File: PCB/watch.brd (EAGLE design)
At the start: 81.1 x 53.1 mm, 58 parts, among them IC1 ISL1209, J2 USB-MICROB, Q1 32.768 KHz, T1 BC850, U2 MKL27Z256VLH4

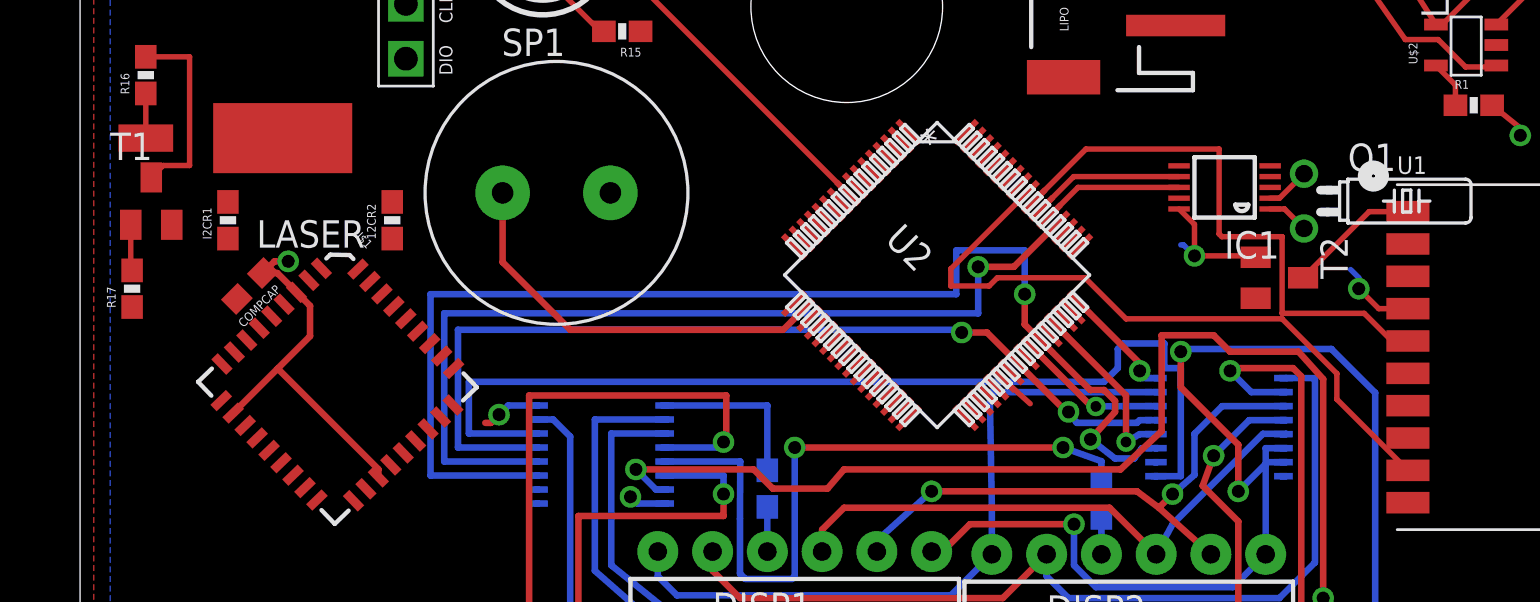
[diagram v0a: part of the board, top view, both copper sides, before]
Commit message: laser wired
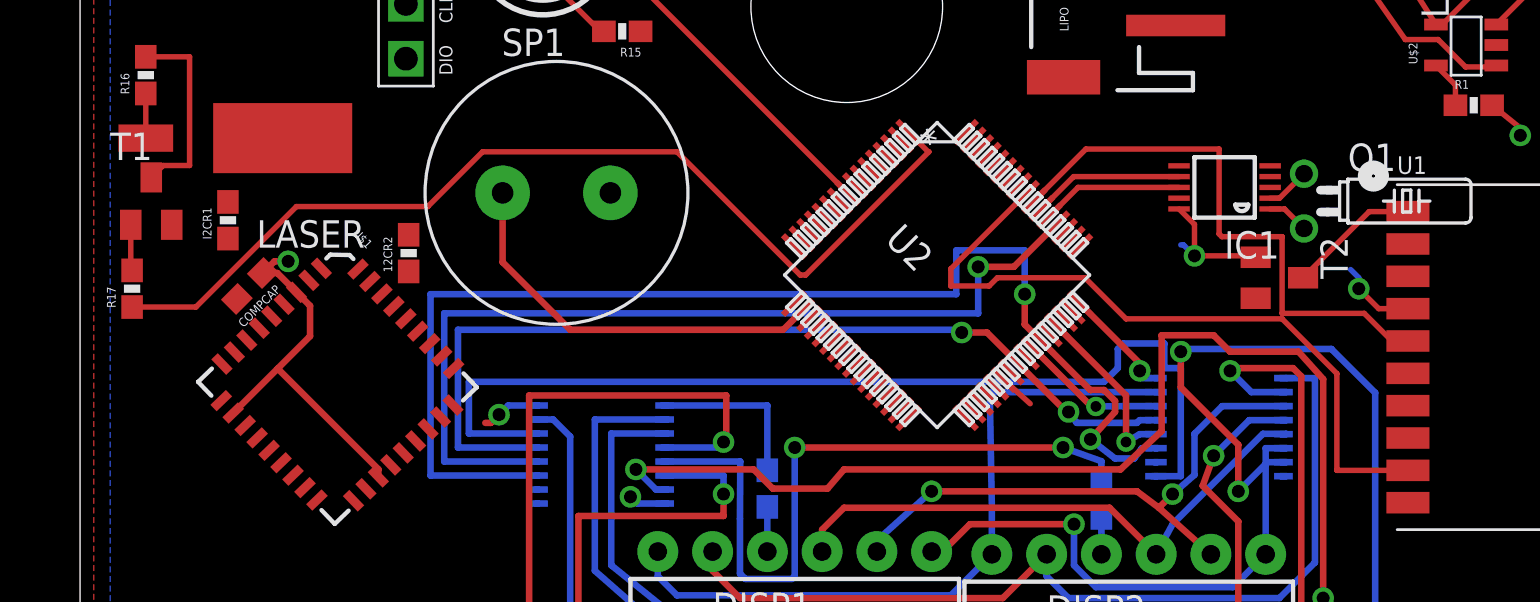
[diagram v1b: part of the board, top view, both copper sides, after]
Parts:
- moved 12CR2 1.70 mm to (26.2, 42.9)
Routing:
- net PTE0: track 0.00 -> 46.0 mm
- net PTC11: track 31.5 -> 33.5 mm
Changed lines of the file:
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@@
 </autorouter>
 <elements>
-<element name="12CR2" library="SparkFun-Resistors" package="0603-RES" value="10K" x="25.4" y="44.45" rot="R90"/>
+<element name="12CR2" library="SparkFun-Resistors" package="0603-RES" value="10K" x="26.162" y="42.926" rot="R90"/>
 <element name="C1" library="SparkFun" package="0603" value=".1uf" x="-41.91" y="73.66"/>
 <element name="C2" library="SparkFun" package="0603" value=".1uf" x="-45.72" y="73.66"/>
@@
 <wire x1="29.718" y1="35.052" x2="24.758084375" y2="32.899915625" width="0" layer="19" extent="1-1"/>
 <wire x1="57.302134375" y1="40.584171875" x2="61.976" y2="43.307" width="0" layer="19" extent="1-16"/>
-<wire x1="25.4" y1="45.3" x2="20.574" y2="42.545" width="0" layer="19" extent="1-1"/>
+<wire x1="26.162" y1="43.776" x2="20.574" y2="42.545" width="0" layer="19" extent="1-1"/>
 <wire x1="48.640065625" y1="35.98796875" x2="57.302134375" y2="40.584171875" width="0" layer="19" extent="1-1"/>
 <wire x1="45.104521875" y1="44.29648125" x2="48.640065625" y2="35.98796875" width="0" layer="19" extent="1-1"/>
@@
 <wire x1="57.2118875" y1="45.974" x2="55.887921875" y2="44.650034375" width="0.254" layer="1"/>
 <wire x1="26.030421875" y1="39.880965625" x2="55.887921875" y2="44.650034375" width="0" layer="19" extent="1-1"/>
-<wire x1="25.4" y1="43.6" x2="26.030421875" y2="39.880965625" width="0" layer="19" extent="1-1"/>
+<wire x1="26.162" y1="42.076" x2="26.030421875" y2="39.880965625" width="0" layer="19" extent="1-1"/>
 </signal>
 <signal name="PTC9">
@@
 <contactref element="R17" pad="1"/>
 <contactref element="U2" pad="1"/>
-<wire x1="13.335" y1="40.425" x2="49.347171875" y2="48.539134375" width="0" layer="19" extent="1-1"/>
+<wire x1="13.335" y1="40.425" x2="16.295" y2="40.425" width="0.254" layer="1"/>
+<wire x1="16.295" y1="40.425" x2="20.955" y2="45.085" width="0.254" layer="1"/>
+<wire x1="29.591" y1="47.625" x2="38.608" y2="47.625" width="0.254" layer="1"/>
+<wire x1="38.608" y1="47.625" x2="44.323" y2="41.91" width="0.254" layer="1"/>
+<wire x1="44.323" y1="41.91" x2="44.577" y2="41.91" width="0.254" layer="1"/>
+<wire x1="44.577" y1="41.91" x2="50.292" y2="47.625" width="0.254" layer="1"/>
+<wire x1="50.292" y1="47.625" x2="50.26130625" y2="47.625" width="0.254" layer="1"/>
+<wire x1="50.26130625" y1="47.625" x2="49.347171875" y2="48.539134375" width="0.254" layer="1"/>
+<wire x1="20.955" y1="45.085" x2="27.051" y2="45.085" width="0.254" layer="1"/>
+<wire x1="27.051" y1="45.085" x2="29.591" y2="47.625" width="0.254" layer="1"/>
 </signal>
 <signal name="PTA18">
@@
 <contactref element="U1" pad="P$9"/>
 <contactref element="U2" pad="56"/>
-<wire x1="72.51" y1="32.85" x2="69.215" y2="36.145" width="0.254" layer="1"/>
-<wire x1="69.215" y1="36.145" x2="69.215" y2="37.338" width="0.254" layer="1"/>
 <wire x1="69.215" y1="37.338" x2="66.675" y2="39.878" width="0.254" layer="1"/>
 <wire x1="66.675" y1="39.878" x2="59.436" y2="39.878" width="0.254" layer="1"/>
@@
 <wire x1="51.308" y1="41.402" x2="51.308" y2="42.1914625" width="0.254" layer="1"/>
 <wire x1="51.308" y1="42.1914625" x2="54.827246875" y2="45.710709375" width="0.254" layer="1"/>
+<wire x1="69.215" y1="37.338" x2="69.215" y2="32.85" width="0.254" layer="1"/>
+<wire x1="69.215" y1="32.85" x2="72.51" y2="32.85" width="0.254" layer="1"/>
 </signal>
 </signals>

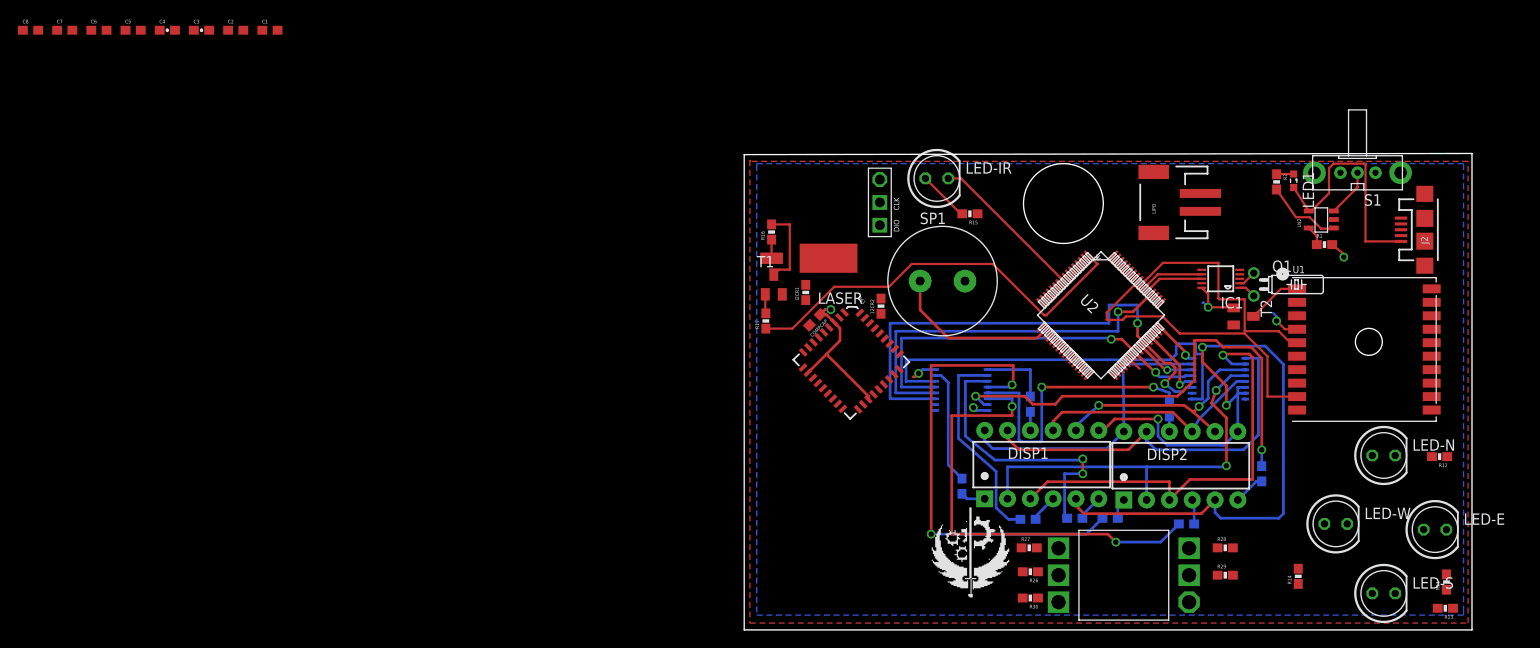
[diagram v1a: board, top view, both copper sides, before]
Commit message: refactored charging circuit and add caps to it
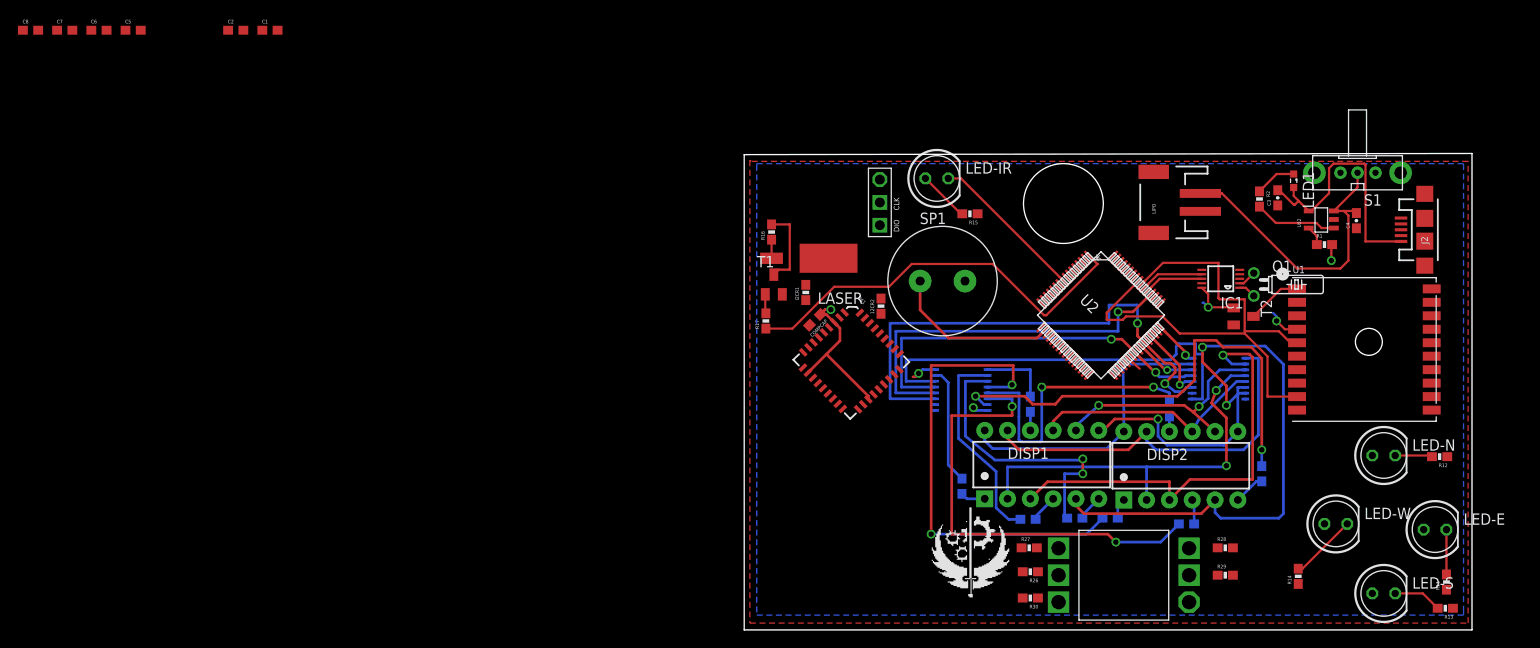
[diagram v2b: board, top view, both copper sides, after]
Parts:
- moved C4 134.1 mm to (79.1, 52.5), turned to 90 degrees
- moved C3 121.3 mm to (70.4, 55.0), turned to 90 degrees
- moved R2 2.69 mm to (68.3, 54.9)
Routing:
- net N$3: track 5.35 -> 34.2 mm
- net N$37: track 0.00 -> 7.53 mm
- net N$38: track 0.00 -> 5.42 mm
- net N$36: track 0.00 -> 4.99 mm
- net N$35: track 0.00 -> 4.16 mm
- net N$4: track 25.8 -> 29.2 mm
- net N$5: track 1.93 -> 4.62 mm
- net N$7: track 8.54 -> 9.27 mm
- net GND: track 4.61 -> 3.89 mm

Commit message: wired compass LEDs. good god this thing is a mess
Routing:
- net PTD2: track 0.00 -> 81.2 mm
- net PTD3: track 0.00 -> 75.6 mm, vias 0 -> 1
- net PTD1: track 0.00 -> 73.4 mm
- net PTD5: track 0.00 -> 70.0 mm, vias 0 -> 1
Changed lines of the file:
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@@
 <contactref element="U2" pad="62"/>
 <contactref element="LED-N" pad="A"/>
-<wire x1="52.70593125" y1="47.832028125" x2="80.899" y2="26.289" width="0" layer="19" extent="1-1"/>
+<wire x1="80.899" y1="26.289" x2="80.899" y2="26.543" width="0.254" layer="16"/>
+<wire x1="80.899" y1="26.543" x2="82.931" y2="28.575" width="0.254" layer="16"/>
+<wire x1="82.931" y1="28.575" x2="87.757" y2="28.575" width="0.254" layer="16"/>
+<wire x1="87.757" y1="28.575" x2="89.408" y2="30.226" width="0.254" layer="16"/>
+<wire x1="89.408" y1="30.226" x2="89.408" y2="49.403" width="0.254" layer="16"/>
+<wire x1="89.408" y1="49.403" x2="86.614" y2="52.197" width="0.254" layer="16"/>
+<wire x1="86.614" y1="52.197" x2="66.929" y2="52.197" width="0.254" layer="16"/>
+<wire x1="66.929" y1="52.197" x2="65.786" y2="51.054" width="0.254" layer="16"/>
+<via x="65.786" y="51.054" extent="1-16" drill="0.6" shape="square"/>
+<wire x1="65.786" y1="51.054" x2="60.706" y2="51.054" width="0.254" layer="1"/>
+<wire x1="60.706" y1="51.054" x2="60.579" y2="51.054" width="0" layer="19" extent="1-16"/>
+<wire x1="52.70593125" y1="47.832028125" x2="54.530903125" y2="49.657" width="0.254" layer="1"/>
+<wire x1="54.530903125" y1="49.657" x2="60.706" y2="49.657" width="0.254" layer="1"/>
+<wire x1="60.706" y1="49.657" x2="60.706" y2="51.054" width="0.254" layer="1"/>
 </signal>
 <signal name="PTD3">
 <contactref element="U2" pad="60"/>
 <contactref element="LED-E" pad="A"/>
-<wire x1="53.413034375" y1="47.124921875" x2="86.614" y2="18.034" width="0" layer="19" extent="1-1"/>
+<wire x1="86.614" y1="18.034" x2="86.614" y2="26.035" width="0.254" layer="16"/>
+<wire x1="86.614" y1="26.035" x2="90.17" y2="29.591" width="0.254" layer="16"/>
+<wire x1="90.17" y1="29.591" x2="90.17" y2="49.657" width="0.254" layer="16"/>
+<wire x1="90.17" y1="49.657" x2="86.106" y2="53.721" width="0.254" layer="16"/>
+<wire x1="86.106" y1="53.721" x2="66.548" y2="53.721" width="0.254" layer="16"/>
+<wire x1="66.548" y1="53.721" x2="64.77" y2="51.943" width="0.254" layer="16"/>
+<wire x1="64.77" y1="51.943" x2="64.77" y2="49.657" width="0.254" layer="16"/>
+<wire x1="64.77" y1="49.657" x2="64.389" y2="49.657" width="0.254" layer="16"/>
+<via x="64.389" y="49.657" extent="1-16" drill="0.6" shape="square"/>
+<wire x1="55.5641125" y1="49.276" x2="53.413034375" y2="47.124921875" width="0.254" layer="1"/>
+<wire x1="55.5641125" y1="49.276" x2="62.865" y2="49.276" width="0.254" layer="1"/>
+<wire x1="62.865" y1="49.276" x2="63.246" y2="49.657" width="0.254" layer="1"/>
+<wire x1="63.246" y1="49.657" x2="64.389" y2="49.657" width="0.254" layer="1"/>
 </signal>
 <signal name="PTD2">
 <contactref element="U2" pad="59"/>
 <contactref element="LED-S" pad="A"/>
-<wire x1="80.899" y1="10.922" x2="53.7665875" y2="46.77136875" width="0" layer="19" extent="1-1"/>
+<wire x1="80.899" y1="10.922" x2="86.614" y2="16.637" width="0.254" layer="1"/>
+<wire x1="86.614" y1="16.637" x2="87.884" y2="16.637" width="0.254" layer="1"/>
+<wire x1="87.884" y1="16.637" x2="88.011" y2="16.764" width="0.254" layer="1"/>
+<wire x1="88.011" y1="16.764" x2="88.011" y2="22.86" width="0.254" layer="1"/>
+<wire x1="88.011" y1="22.86" x2="90.17" y2="25.019" width="0.254" layer="1"/>
+<wire x1="90.17" y1="25.019" x2="90.17" y2="29.718" width="0.254" layer="1"/>
+<wire x1="90.17" y1="29.718" x2="89.408" y2="30.48" width="0.254" layer="1"/>
+<wire x1="89.408" y1="30.48" x2="89.408" y2="48.895" width="0.254" layer="1"/>
+<wire x1="89.408" y1="48.895" x2="89.281" y2="48.768" width="0.254" layer="1"/>
+<wire x1="89.281" y1="48.768" x2="80.645" y2="48.768" width="0.254" layer="1"/>
+<wire x1="80.645" y1="48.768" x2="78.613" y2="46.736" width="0.254" layer="1"/>
+<wire x1="78.613" y1="46.736" x2="71.374" y2="46.736" width="0.254" layer="1"/>
+<wire x1="71.374" y1="46.736" x2="69.342" y2="48.768" width="0.254" layer="1"/>
+<wire x1="69.342" y1="48.768" x2="55.626" y2="48.768" width="0.254" layer="1"/>
+<wire x1="55.626" y1="48.768" x2="53.7665875" y2="46.9085875" width="0.254" layer="1"/>
+<wire x1="53.7665875" y1="46.9085875" x2="53.7665875" y2="46.77136875" width="0.254" layer="1"/>
 </signal>
 <signal name="PTD1">
 <contactref element="U2" pad="58"/>
 <contactref element="LED-W" pad="A"/>
-<wire x1="75.565" y1="18.669" x2="54.120140625" y2="46.41781875" width="0" layer="19" extent="1-1"/>
+<wire x1="75.565" y1="18.669" x2="82.423" y2="25.527" width="0.254" layer="1"/>
+<wire x1="82.423" y1="25.527" x2="82.423" y2="28.829" width="0.254" layer="1"/>
+<wire x1="82.423" y1="28.829" x2="83.058" y2="29.464" width="0.254" layer="1"/>
+<wire x1="83.058" y1="29.464" x2="88.519" y2="29.464" width="0.254" layer="1"/>
+<wire x1="88.519" y1="29.464" x2="89.408" y2="30.353" width="0.254" layer="1"/>
+<wire x1="89.408" y1="30.353" x2="89.408" y2="45.974" width="0.254" layer="1"/>
+<wire x1="89.408" y1="45.974" x2="89.281" y2="46.101" width="0.254" layer="1"/>
+<wire x1="89.281" y1="46.101" x2="70.358" y2="46.101" width="0.254" layer="1"/>
+<wire x1="70.358" y1="46.101" x2="68.072" y2="48.387" width="0.254" layer="1"/>
+<wire x1="68.072" y1="48.387" x2="56.007" y2="48.387" width="0.254" layer="1"/>
+<wire x1="56.007" y1="48.387" x2="54.120140625" y2="46.500140625" width="0.254" layer="1"/>
+<wire x1="54.120140625" y1="46.500140625" x2="54.120140625" y2="46.41781875" width="0.254" layer="1"/>
 </signal>
 <signal name="N$39">

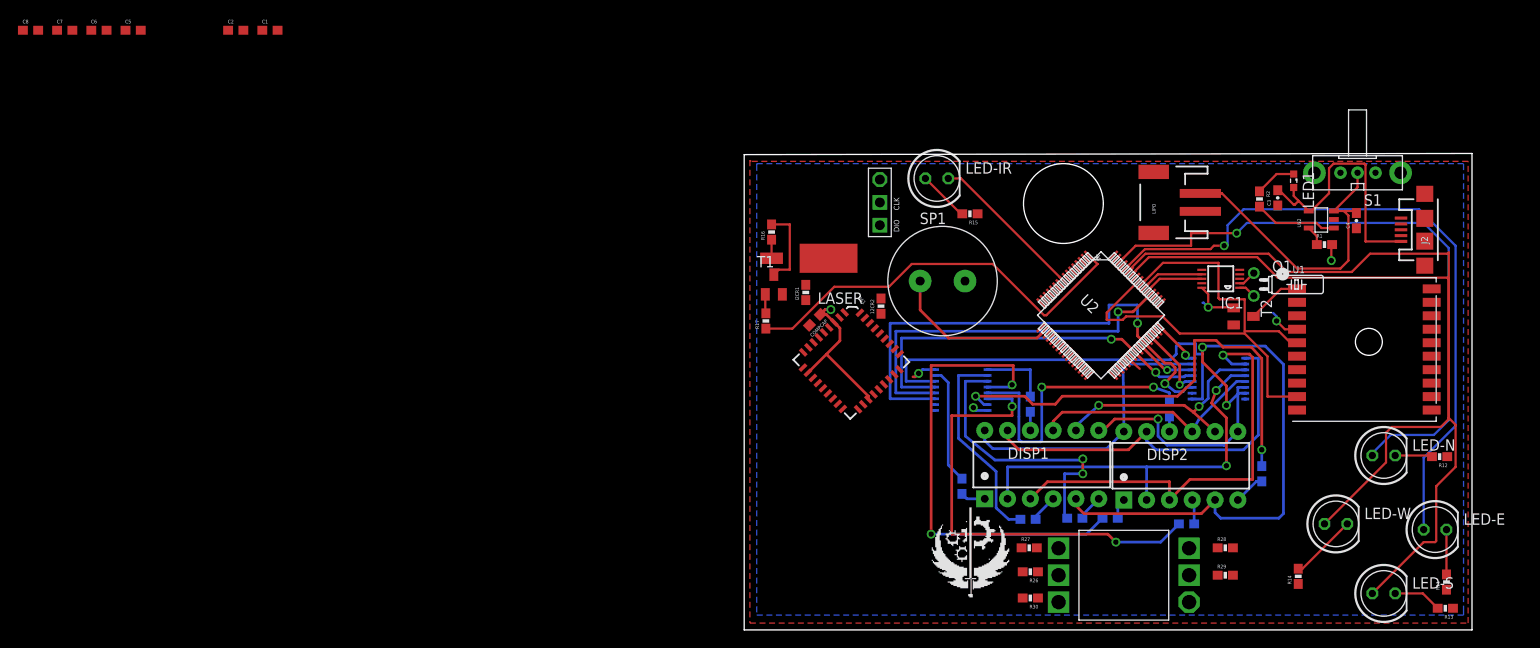
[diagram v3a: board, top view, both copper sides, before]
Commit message: removed airwires, added decoupling caps
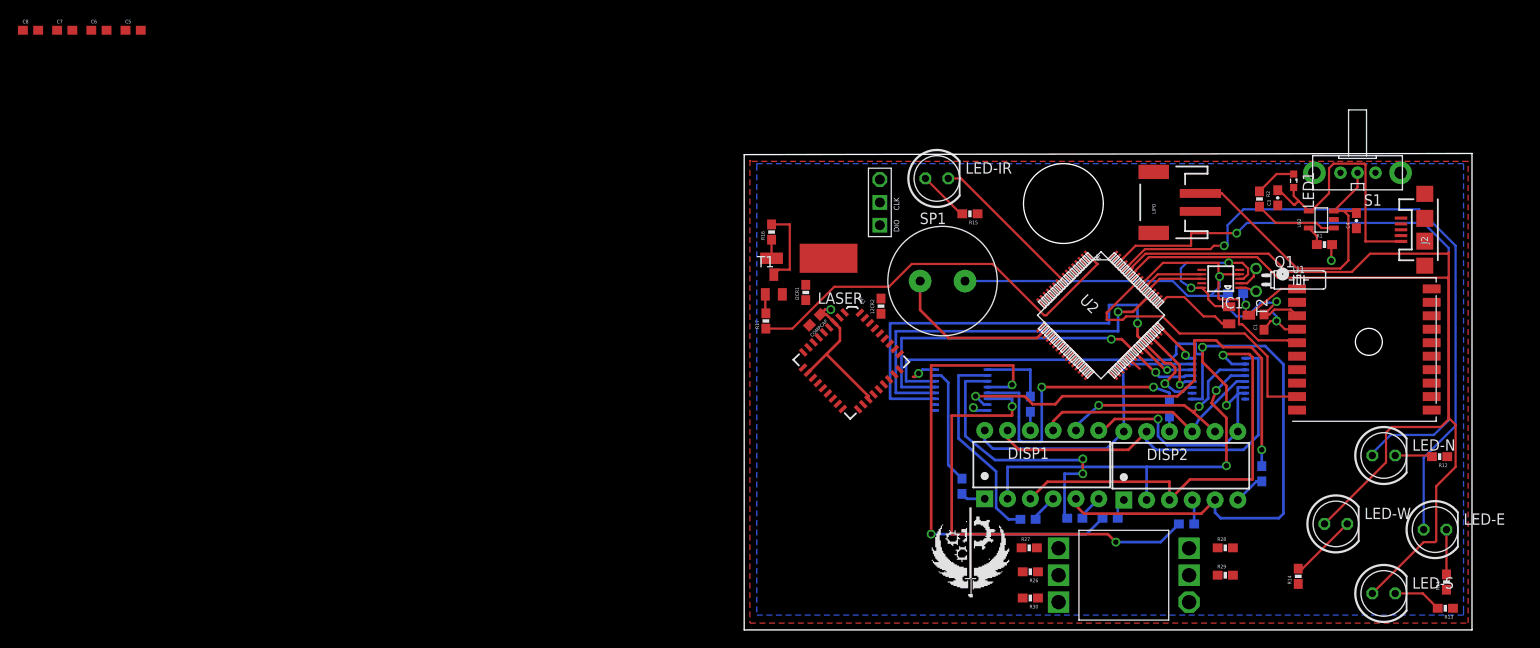
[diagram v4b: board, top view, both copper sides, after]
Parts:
- moved C1 115.4 mm to (68.8, 41.1), turned to 90 degrees
- moved C2 115.2 mm to (65.7, 44.3), flipped to the bottom
- moved Q1 0.57 mm to (67.9, 45.8)
- moved T2 0.52 mm to (66.0, 41.9)
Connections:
- new net PTC4: T2.B, U2.49
- net PTA18: no longer T2.B
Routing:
- net GND: track 3.89 -> 53.2 mm, vias 2 -> 4
- net V+: track 35.2 -> 49.4 mm, vias 5 -> 6
- net PTC4: track 0.00 -> 9.17 mm
- net N$6: track 6.13 -> 9.05 mm, vias 0 -> 1
- net N$44: track 2.04 -> 2.88 mm

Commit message: wired swd
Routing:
- net PTA3: track 0.00 -> 39.8 mm, vias 0 -> 1
- net PTA0: track 0.00 -> 38.8 mm, vias 0 -> 1
